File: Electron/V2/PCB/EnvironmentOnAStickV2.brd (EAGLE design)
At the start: 92.7 x 31.8 mm, 15 parts, among them U1 HTU21DSMD, U2 BMP180, U4 LIGHTSENSORTEMT6000

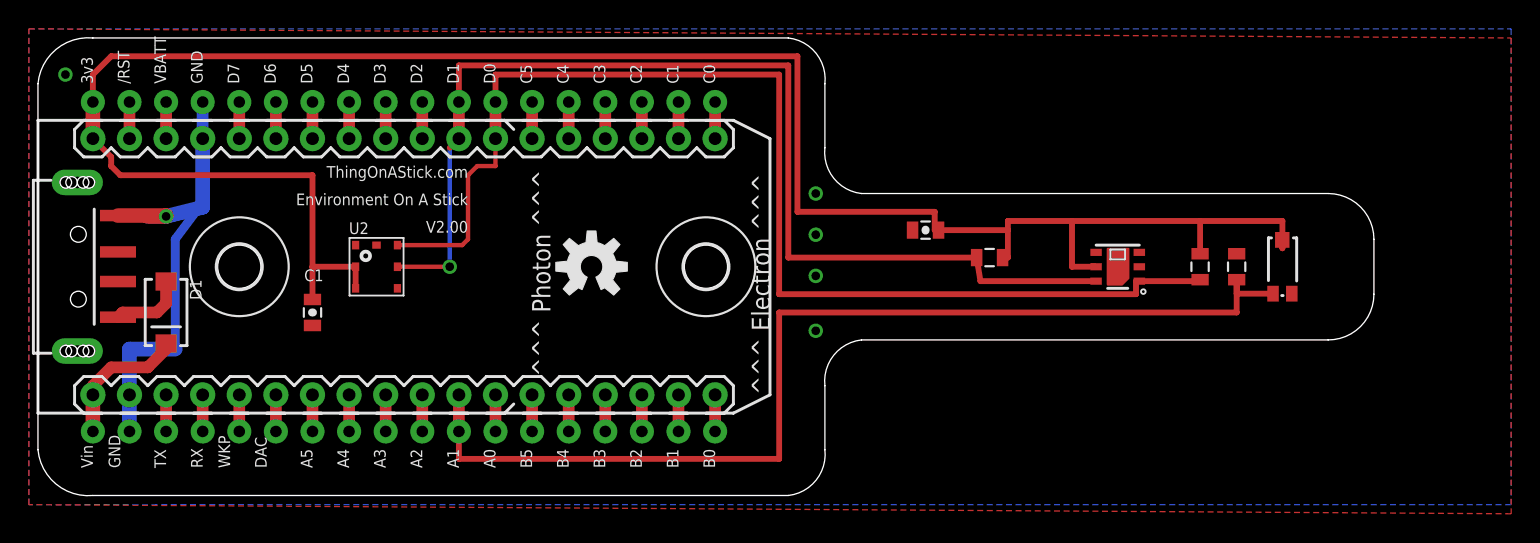
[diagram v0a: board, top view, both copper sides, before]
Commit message: Added reverse mount LED to V2 environment stick and moved OSH logo to cover it.
Exported PCB/schema to pdf and images.

Added datasheet for BMP180
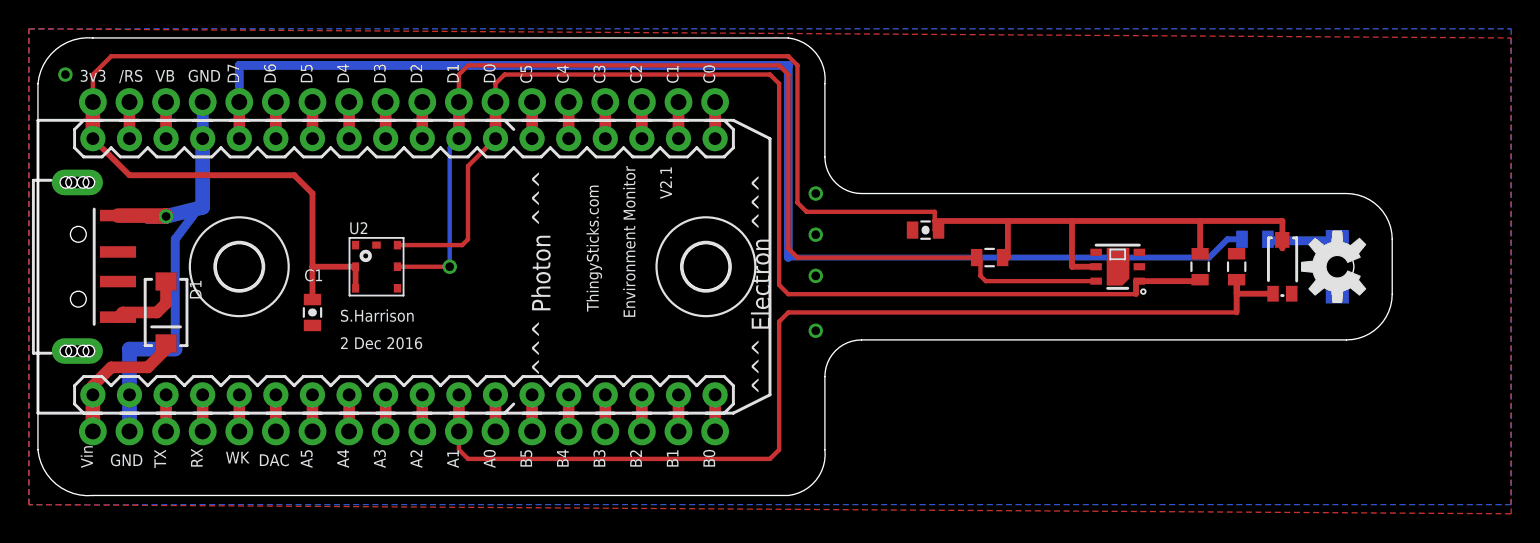
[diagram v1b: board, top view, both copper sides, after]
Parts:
- added D2: (no value), SparkFun-LED:LED-1206-BOTTOM
- added R1: 310R, SparkFun-Resistors:0805
- H1, H2: value MOUNT-HOLE3.0 -> MOUNT-HOLE3.2; device holes:3,0 -> holes:3,2
- moved LOGO1 51.8 mm to (90.2, 15.9), turned to 90 degrees
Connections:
- removed net N$3: U$1.D7, U$1.D7_1
- new net N$6: D2.A, R1.1
- new net OSHLED: R1.2, U$1.D7, U$1.D7_1
- net GND: now also D2.C
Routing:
- net OSHLED: track 0.00 -> 88.5 mm
- net N$6: track 0.00 -> 4.92 mm
- net N$3: track 2.54 -> 0.00 mm
- net SCL: track 77.7 -> 75.6 mm
- net SDA: track 83.2 -> 81.3 mm
- net 3.3V: track 141.9 -> 140.3 mm
- net LIGHTLEVEL_ANALOG: track 74.3 -> 73.2 mm
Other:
- board size 92.7 x 31.8 mm -> 94 x 31.8 mm
- board text added: "2 Dec 2016"
- board text added: "Environment Monitor"
- board text added: "S.Harrison"
- board text added: "ThingySticks.com"
- board text added: "V2.1"
- board text removed: "Environment On A Stick"
- board text removed: "ThingOnAStick.com"
- board text removed: "V2.00"
